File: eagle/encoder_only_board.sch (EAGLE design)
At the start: 27 parts, among them IC2 AT42QT1010SOT23, J1 FH12-6S-0.5SH(55), J2 FH12-6S-0.5SH(55)

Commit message: Update switch voltage divider and connect encoder touch to it
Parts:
- added R6: 0, rcl:R-EU_R0603
- R24: value 0 -> 10k
- R4: value 10k -> 100k
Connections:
- removed net N$2: R2.2, R3.2, R4.1
- removed net SW1: J1.1, J2.6, R24.2, R27.2, R28.2
- new net SW_IN: J1.1, R27.2, R28.2, R6.1
- new net SW_OUT: J2.6, R3.2
- net ENC_SW: now also R3.1, R4.1
- net ENC_SW_PU: now also R24.2, R6.2; no longer R3.1
- net GND: now also R2.2
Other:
- note added: "Feature jumpers"
- note removed: "POT jumpers"

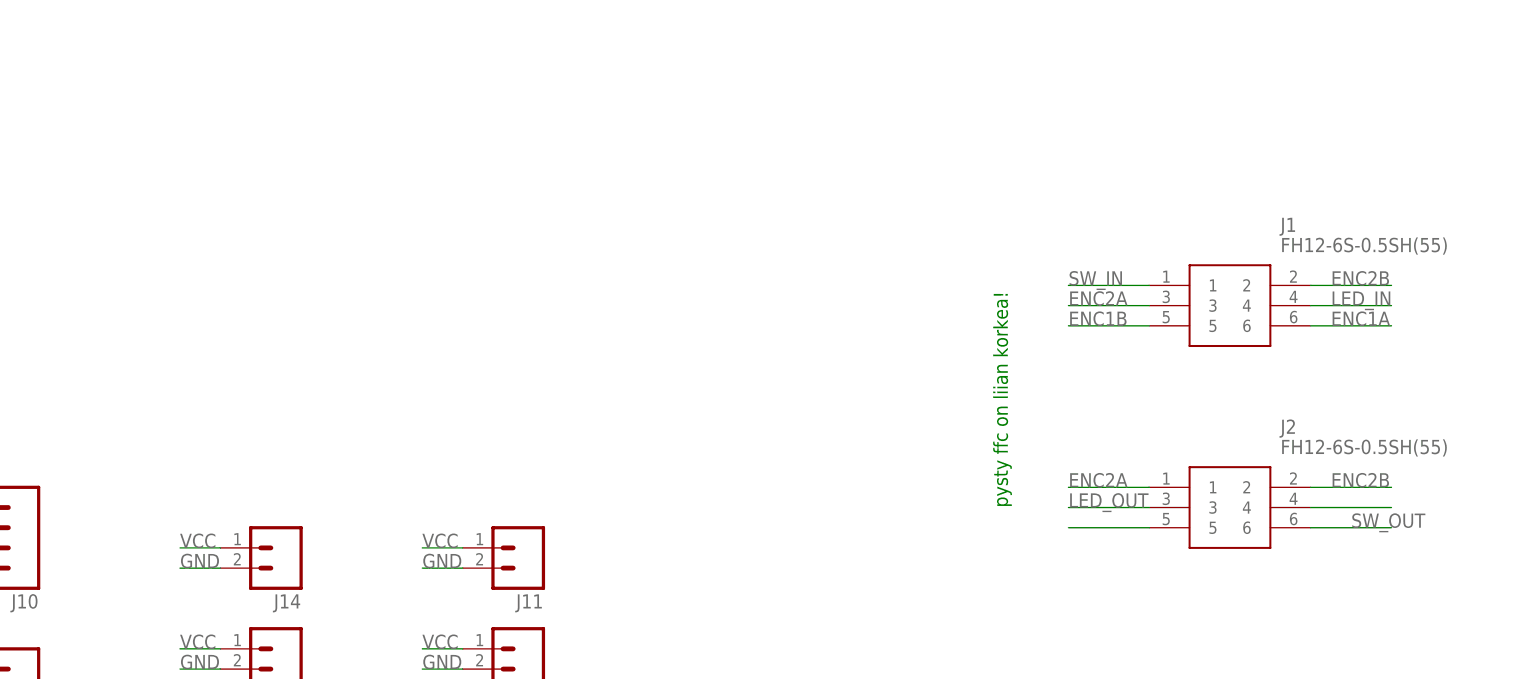
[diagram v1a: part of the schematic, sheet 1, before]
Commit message: Board version 4 WIP;
* Added solder pads to FFC connectors
* Fixed naming of connectors (previously M was on the right and labels
  were wrong
* Flipped builtin led (D1) around to make it safer to use with encoders
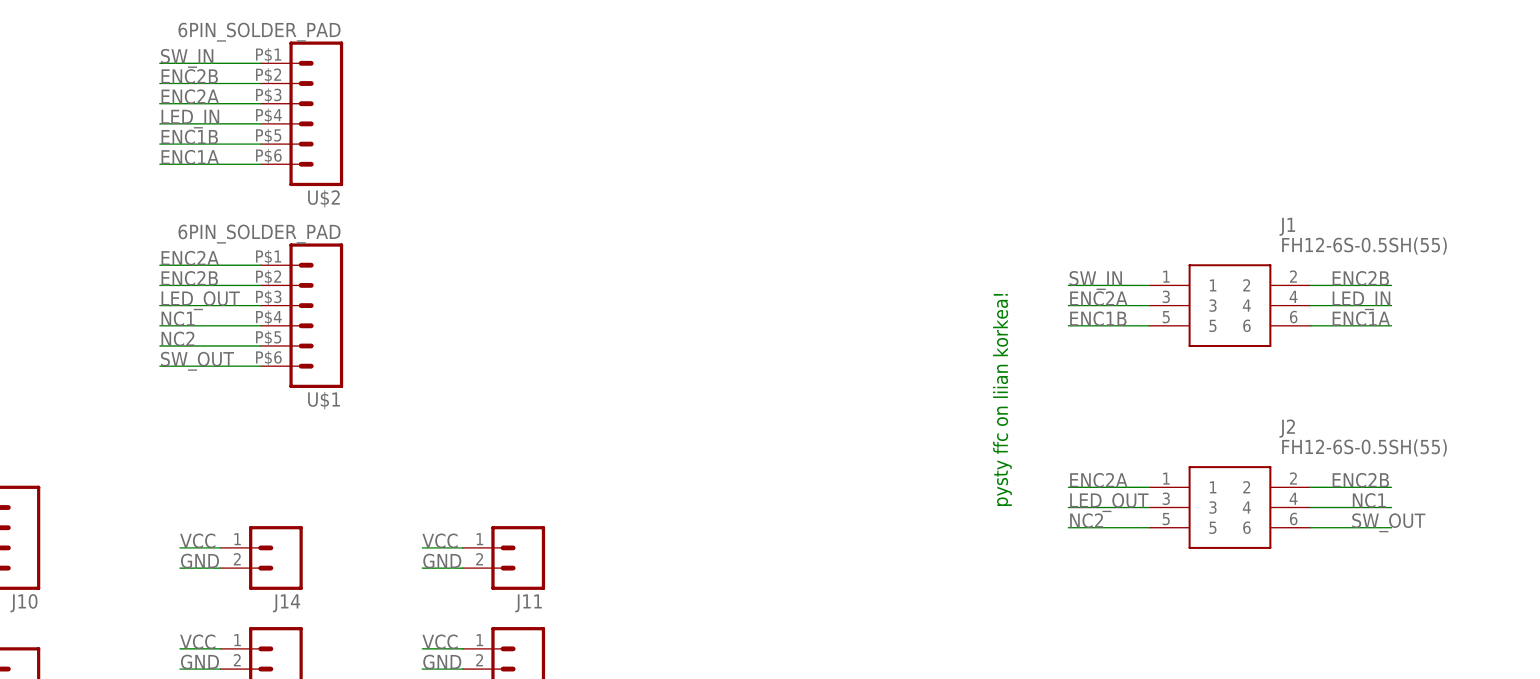
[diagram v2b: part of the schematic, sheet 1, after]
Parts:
- added U$1, U$2: 6PIN_SOLDER_PAD, edge:6PIN_SOLDER_PAD
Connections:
- removed net N$10: J2.4
- removed net N$14: J2.5
- new net NC1: J2.4, U$1.4
- new net NC2: J2.5, U$1.5
- net ENC1A: now also U$2.6
- net ENC1B: now also U$2.5
- net ENC2A: now also U$1.1, U$2.3
- net ENC2B: now also U$1.2, U$2.2
- net LED_IN: now also U$2.4
- net LED_OUT: now also U$1.3
- net SW_IN: now also U$2.1
- net SW_OUT: now also U$1.6
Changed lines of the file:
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@@
 <attribute name="SPICEPREFIX" value="R"/>
 </part>
+<part name="R6" library="rcl" deviceset="R-EU_" device="R0603" value="0">
+<attribute name="SPICEPREFIX" value="R"/>
+</part>
+<part name="U$1" library="edge" deviceset="6PIN_SOLDER_PAD" device=""/>
+<part name="U$2" library="edge" deviceset="6PIN_SOLDER_PAD" device=""/>
 <part name="R3" library="rcl" deviceset="R-EU_" device="R0603" value="10k">
 <attribute name="SPICEPREFIX" value="R"/>
 </part>
 <part name="R4" library="rcl" deviceset="R-EU_" device="R0603" value="100k">
-<attribute name="SPICEPREFIX" value="R"/>
-</part>
-<part name="R6" library="rcl" deviceset="R-EU_" device="R0603" value="0">
 <attribute name="SPICEPREFIX" value="R"/>
 </part>
@@
 <attribute name="VALUE" x="67.31" y="-147.32" size="1.778" layer="96" align="center-left"/>
 </instance>
+<instance part="U$1" gate="G$1" x="-55.88" y="-129.54" smashed="yes" rot="R180">
+<attribute name="VALUE" x="-50.8" y="-119.38" size="1.778" layer="96" rot="R180"/>
+<attribute name="NAME" x="-50.8" y="-140.462" size="1.778" layer="95" rot="R180"/>
+</instance>
+<instance part="U$2" gate="G$1" x="-55.88" y="-104.14" smashed="yes" rot="R180">
+<attribute name="VALUE" x="-50.8" y="-93.98" size="1.778" layer="96" rot="R180"/>
+<attribute name="NAME" x="-50.8" y="-115.062" size="1.778" layer="95" rot="R180"/>
+</instance>
 </instances>
 <busses>
@@
 <label x="40.64" y="-154.94" size="1.778" layer="95"/>
 </segment>
+<segment>
+<pinref part="U$1" gate="G$1" pin="3"/>
+<wire x1="-60.96" y1="-129.54" x2="-73.66" y2="-129.54" width="0.1524" layer="91"/>
+<label x="-73.66" y="-129.54" size="1.778" layer="95"/>
+</segment>
 </net>
 <net name="ENC1A" class="0">
@@
 <label x="73.66" y="-132.08" size="1.778" layer="95"/>
 </segment>
+<segment>
+<pinref part="U$2" gate="G$1" pin="6"/>
+<wire x1="-60.96" y1="-111.76" x2="-73.66" y2="-111.76" width="0.1524" layer="91"/>
+<label x="-73.66" y="-111.76" size="1.778" layer="95"/>
+</segment>
 </net>
 <net name="ENC1B" class="0">
@@
 <label x="40.64" y="-132.08" size="1.778" layer="95"/>
 </segment>
+<segment>
+<pinref part="U$2" gate="G$1" pin="5"/>
+<wire x1="-60.96" y1="-109.22" x2="-73.66" y2="-109.22" width="0.1524" layer="91"/>
+<label x="-73.66" y="-109.22" size="1.778" layer="95"/>
+</segment>
 </net>
 <net name="LED_IN" class="0">
@@
 <label x="73.66" y="-129.54" size="1.778" layer="95"/>
 </segment>
+<segment>
+<pinref part="U$2" gate="G$1" pin="4"/>
+<wire x1="-60.96" y1="-106.68" x2="-73.66" y2="-106.68" width="0.1524" layer="91"/>
+<label x="-73.66" y="-106.68" size="1.778" layer="95"/>
+</segment>
 </net>
 <net name="ENC2B" class="0">
@@
 <label x="73.66" y="-127" size="1.778" layer="95"/>
 </segment>
+<segment>
+<pinref part="U$2" gate="G$1" pin="2"/>
+<wire x1="-60.96" y1="-101.6" x2="-73.66" y2="-101.6" width="0.1524" layer="91"/>
+<label x="-73.66" y="-101.6" size="1.778" layer="95"/>
+</segment>
+<segment>
+<pinref part="U$1" gate="G$1" pin="2"/>
+<wire x1="-60.96" y1="-127" x2="-73.66" y2="-127" width="0.1524" layer="91"/>
+<label x="-73.66" y="-127" size="1.778" layer="95"/>
+</segment>
 </net>
 <net name="POT" class="0">
@@
 <label x="40.64" y="-129.54" size="1.778" layer="95"/>
 </segment>
+<segment>
+<pinref part="U$2" gate="G$1" pin="3"/>
+<wire x1="-60.96" y1="-104.14" x2="-73.66" y2="-104.14" width="0.1524" layer="91"/>
+<label x="-73.66" y="-104.14" size="1.778" layer="95"/>
+</segment>
+<segment>
+<pinref part="U$1" gate="G$1" pin="1"/>
+<wire x1="-60.96" y1="-124.46" x2="-73.66" y2="-124.46" width="0.1524" layer="91"/>
+<label x="-73.66" y="-124.46" size="1.778" layer="95"/>
+</segment>
 </net>
 <net name="SW_IN" class="0">
@@
 <label x="40.64" y="-127" size="1.778" layer="95"/>
 </segment>
+<segment>
+<pinref part="U$2" gate="G$1" pin="1"/>
+<wire x1="-60.96" y1="-99.06" x2="-73.66" y2="-99.06" width="0.1524" layer="91"/>
+<label x="-73.66" y="-99.06" size="1.778" layer="95"/>
+</segment>
 </net>
 <net name="ENC_SW_PU" class="0">
@@
 </segment>
 </net>
-<net name="N$10" class="0">
+<net name="NC1" class="0">
 <segment>
 <pinref part="J2" gate="G$1" pin="4"/>
 <wire x1="71.12" y1="-154.94" x2="81.28" y2="-154.94" width="0.1524" layer="91"/>
-</segment>
-</net>
-<net name="N$14" class="0">
+<label x="76.2" y="-154.94" size="1.778" layer="95"/>
+</segment>
+<segment>
+<pinref part="U$1" gate="G$1" pin="4"/>
+<wire x1="-60.96" y1="-132.08" x2="-73.66" y2="-132.08" width="0.1524" layer="91"/>
+<label x="-73.66" y="-132.08" size="1.778" layer="95"/>
+</segment>
+</net>
+<net name="NC2" class="0">
 <segment>
 <pinref part="J2" gate="G$1" pin="5"/>
 <wire x1="50.8" y1="-157.48" x2="40.64" y2="-157.48" width="0.1524" layer="91"/>
+<label x="40.64" y="-157.48" size="1.778" layer="95"/>
+</segment>
+<segment>
+<pinref part="U$1" gate="G$1" pin="5"/>
+<wire x1="-60.96" y1="-134.62" x2="-73.66" y2="-134.62" width="0.1524" layer="91"/>
+<label x="-73.66" y="-134.62" size="1.778" layer="95"/>
 </segment>
 </net>
@@
 <wire x1="71.12" y1="-157.48" x2="81.28" y2="-157.48" width="0.1524" layer="91"/>
 <label x="76.2" y="-157.48" size="1.778" layer="95"/>
+</segment>
+<segment>
+<pinref part="U$1" gate="G$1" pin="6"/>
+<wire x1="-60.96" y1="-137.16" x2="-73.66" y2="-137.16" width="0.1524" layer="91"/>
+<label x="-73.66" y="-137.16" size="1.778" layer="95"/>
 </segment>
 </net>
@@
 </segment>
 <segment>
+<pinref part="R24" gate="G$1" pin="2"/>
+<wire x1="218.44" y1="48.26" x2="231.14" y2="48.26" width="0.1524" layer="91"/>
+<label x="233.68" y="45.72" size="1.778" layer="95" rot="R180"/>
 <pinref part="R6" gate="G$1" pin="2"/>
-<wire x1="231.14" y1="48.26" x2="223.52" y2="48.26" width="0.1524" layer="91"/>
-</segment>
-<segment>
-<pinref part="R24" gate="G$1" pin="2"/>
-<wire x1="218.44" y1="48.26" x2="226.06" y2="48.26" width="0.1524" layer="91"/>
-<label x="233.68" y="45.72" size="1.778" layer="95" rot="R180"/>
 </segment>
 </net>
@@
 </segment>
 <segment>
-<pinref part="R4" gate="G$1" pin="2"/>
 <wire x1="-38.1" y1="22.86" x2="-38.1" y2="17.78" width="0.1524" layer="91"/>
 <label x="-35.56" y="17.78" size="1.778" layer="95"/>
+<pinref part="R4" gate="G$1" pin="2"/>
 </segment>
 </net>
@@
 </segment>
 </net>
+<net name="SW_OUT" class="0">
+<segment>
+<wire x1="-25.4" y1="22.86" x2="-15.24" y2="22.86" width="0.1524" layer="91"/>
+<label x="-20.32" y="22.86" size="1.778" layer="95"/>
+<pinref part="R3" gate="G$1" pin="2"/>
+</segment>
+</net>
 <net name="ENC_SW" class="0">
 <segment>
 <pinref part="ENC1" gate="G$2" pin="2"/>
+<pinref part="R3" gate="G$1" pin="1"/>
 <wire x1="-20.32" y1="35.56" x2="-25.4" y2="35.56" width="0.1524" layer="91"/>
-<label x="-45.72" y="35.56" size="1.778" layer="95"/>
-<pinref part="R3" gate="G$1" pin="1"/>
+<wire x1="-25.4" y1="33.02" x2="-25.4" y2="35.56" width="0.1524" layer="91"/>
 <wire x1="-25.4" y1="35.56" x2="-38.1" y2="35.56" width="0.1524" layer="91"/>
-<wire x1="-38.1" y1="35.56" x2="-45.72" y2="35.56" width="0.1524" layer="91"/>
-<wire x1="-25.4" y1="35.56" x2="-25.4" y2="33.02" width="0.1524" layer="91"/>
 <pinref part="R4" gate="G$1" pin="1"/>
 <wire x1="-38.1" y1="33.02" x2="-38.1" y2="35.56" width="0.1524" layer="91"/>
-</segment>
-</net>
-<net name="SW_OUT" class="0">
-<segment>
-<pinref part="R3" gate="G$1" pin="2"/>
-<wire x1="-25.4" y1="22.86" x2="-17.78" y2="22.86" width="0.1524" layer="91"/>
-<label x="-20.32" y="22.86" size="1.778" layer="95"/>
-</segment>
-</net>
+<wire x1="-38.1" y1="35.56" x2="-45.72" y2="35.56" width="0.1524" layer="91"/>
+<label x="-45.72" y="35.56" size="1.778" layer="95"/>
+</segment>
+</net>

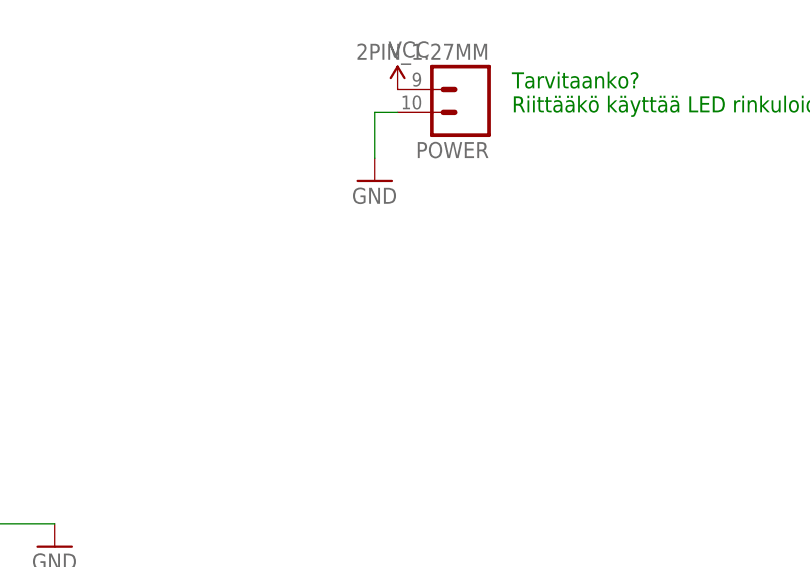
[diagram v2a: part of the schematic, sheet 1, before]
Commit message: Add second power connector for chaining encoder boards
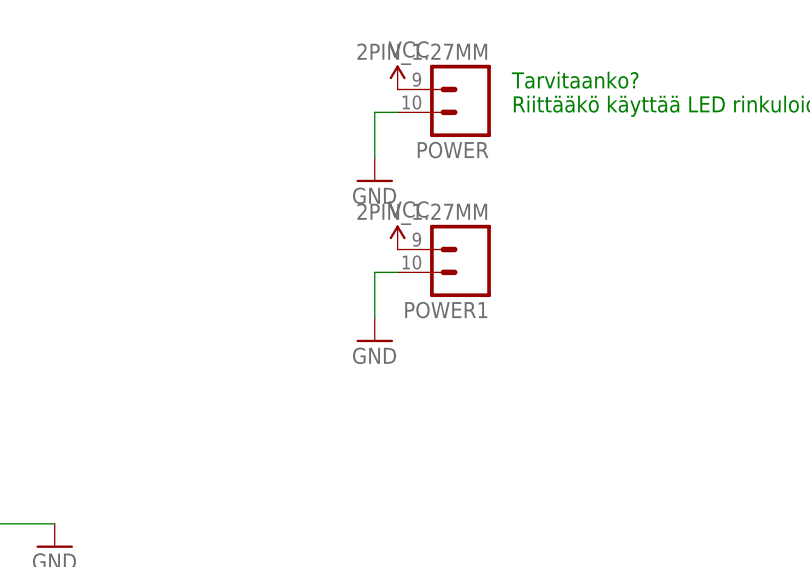
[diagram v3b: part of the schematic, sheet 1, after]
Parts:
- added POWER1: 2PIN_1.27MM, edge:2PIN_1.27MM
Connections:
- net GND: now also POWER1.2
- net VCC: now also POWER1.1
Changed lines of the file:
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@@
 <attribute name="SPICEPREFIX" value="R"/>
 </part>
+<part name="POWER1" library="edge" deviceset="2PIN_1.27MM" device=""/>
+<part name="GND1" library="SparkFun-Aesthetics" deviceset="GND" device=""/>
+<part name="SUPPLY2" library="SparkFun-Aesthetics" deviceset="VCC" device=""/>
 </parts>
 <sheets>
@@
 <attribute name="NAME" x="-50.8" y="-115.062" size="1.778" layer="95" rot="R180"/>
 </instance>
+<instance part="POWER1" gate="G$1" x="154.94" y="-172.72" smashed="yes" rot="R180">
+<attribute name="VALUE" x="157.48" y="-167.64" size="1.778" layer="96" rot="R180"/>
+<attribute name="NAME" x="157.48" y="-178.562" size="1.778" layer="95" rot="R180"/>
+</instance>
+<instance part="GND1" gate="1" x="144.78" y="-182.88" smashed="yes">
+<attribute name="VALUE" x="142.24" y="-185.42" size="1.778" layer="96"/>
+</instance>
+<instance part="SUPPLY2" gate="G$1" x="147.32" y="-172.72" smashed="yes">
+<attribute name="VALUE" x="146.304" y="-169.164" size="1.778" layer="96"/>
+</instance>
 </instances>
 <busses>
@@
 <pinref part="GND11" gate="1" pin="GND"/>
 </segment>
+<segment>
+<pinref part="POWER1" gate="G$1" pin="2"/>
+<pinref part="GND1" gate="1" pin="GND"/>
+<wire x1="147.32" y1="-175.26" x2="144.78" y2="-175.26" width="0.1524" layer="91"/>
+<wire x1="144.78" y1="-175.26" x2="144.78" y2="-180.34" width="0.1524" layer="91"/>
+</segment>
 </net>
 <net name="VCC" class="0">
@@
 <label x="-40.64" y="-160.02" size="1.778" layer="95"/>
 </segment>
+<segment>
+<pinref part="POWER1" gate="G$1" pin="1"/>
+<pinref part="SUPPLY2" gate="G$1" pin="VCC"/>
+</segment>
 </net>

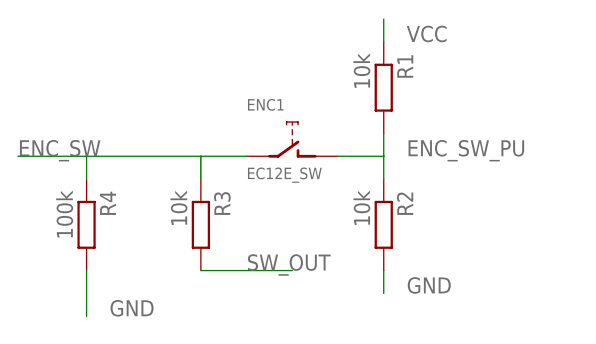
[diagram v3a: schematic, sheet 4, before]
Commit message: Add documentation for encoder only board button voltage divider
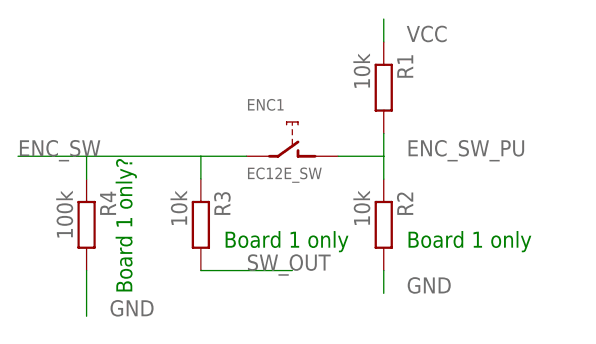
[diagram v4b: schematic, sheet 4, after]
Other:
- note added: "Board 1 only"
- note added: "Board 1 only?"
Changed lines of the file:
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@@
 <sheet>
 <plain>
+<text x="-22.86" y="25.4" size="1.778" layer="91">Board 1 only</text>
+<text x="-2.54" y="25.4" size="1.778" layer="91">Board 1 only</text>
+<text x="-33.02" y="20.32" size="1.778" layer="91" rot="R90">Board 1 only?</text>
 </plain>
 <instances>
